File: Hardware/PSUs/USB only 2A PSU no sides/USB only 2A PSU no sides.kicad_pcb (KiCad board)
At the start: 4 copper layers, 45 x 20 mm, 46 parts, among them J10 G-Switch-GT-USB-7025, J11 1.27mm 4 pin socket, J12 USB, J3 Keystone 3579, J5 Keystone 3569, J7 Keystone 3579, J9 Keystone 3569, U1 AP63205WU, U2 AP63203WU, U5 THVD1420DRLR, U6 CH32X035G8U6, U7 TPS7A2633DRV

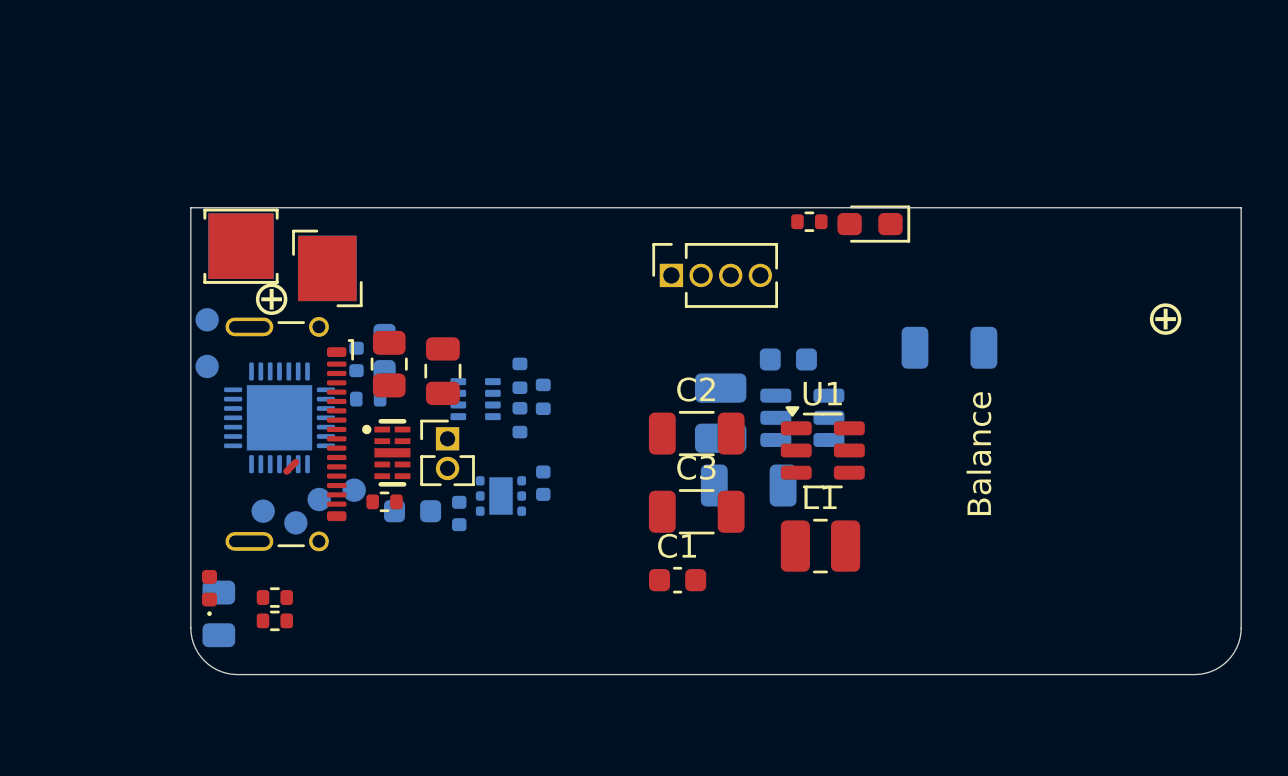
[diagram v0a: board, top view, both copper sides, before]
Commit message: Finished schematic, started arrangement
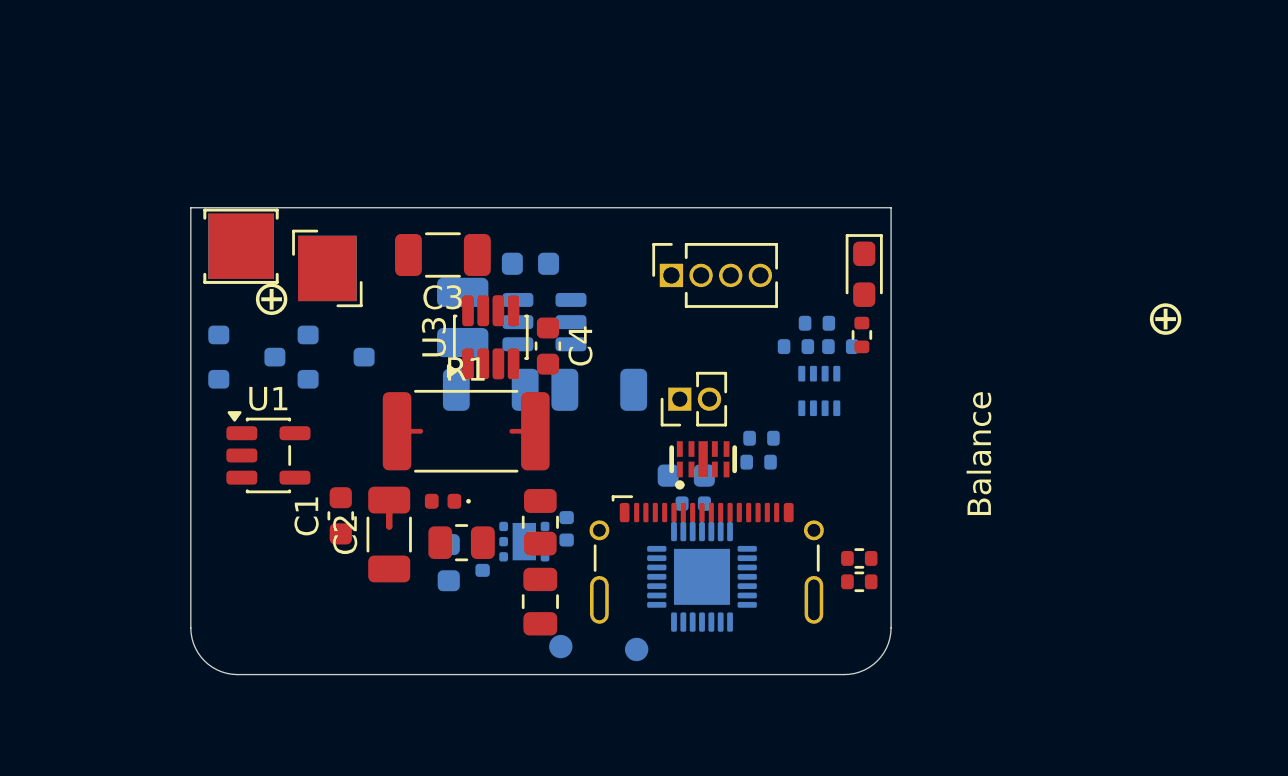
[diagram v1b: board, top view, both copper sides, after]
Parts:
- removed L1: 2.2uH, WIP322512A-2R2MLDG, Inductor_SMD:L_1008_2520Metric
- removed the TP2 at (115.1, 124.1)
- removed TP3: SCK, TestPoint:TestPoint_Pad_D1.0mm
- removed TP5: SDI, TestPoint:TestPoint_Pad_D1.0mm
- removed TP6: SDO, TestPoint:TestPoint_Pad_D1.0mm
- added C4: 100nF, 16v, Capacitor_SMD:C_0603_1608Metric, F.Cu at (123.4, 117.9)
- added NT1: NetTie_2, custom_Connector:NetTie-2_SMD_Pad0.2mm, F.Cu at (117.8, 121.6)
- added NT2: NetTie_2, custom_Connector:NetTie-2_SMD_Pad0.2mm, F.Cu at (122.0, 121.6)
- added Q1: PJA3430, or HL 2320A, Package_TO_SOT_SMD:SC-59, B.Cu at (114.3, 118.4)
- added Q2: PJA3430, or HL 2320A, Package_TO_SOT_SMD:SC-59, B.Cu at (110.5, 118.4)
- added R1: 50mOhm, Resistor_SMD:R_2512_6332Metric, F.Cu at (119.9, 121.6)
- added U3: INA219AxDCN, Package_TO_SOT_SMD:SOT-23-8, F.Cu at (121.0, 117.5)
- C1: value 100nF, 16v -> 10uF, 16v
- R19: moved to B.Cu
- R9: moved to F.Cu
- U1: value AP63205WU -> FAN3111E; footprint Package_TO_SOT_SMD:TSOT-23-6 -> Package_TO_SOT_SMD:SOT-23-5
- U4: renamed from U6; footprint Package_DFN_QFN:QFN-28-1EP_4x4mm_P0.4mm_EP2.8x2.8mm -> Package_DFN_QFN:QFN-28-1EP_4x4mm_P0.4mm_EP2.4x2.4mm
- moved R3 25.2 mm to (136.7, 127.0), turned to 0 degrees
- moved R4 25.0 mm to (136.7, 128.0), turned to 0 degrees
- moved U1 23.8 mm to (111.4, 122.6)
- moved TP2 22.0 mm to (127.2, 130.9), turned to -90 degrees
- moved TP1 20.6 mm to (124.0, 130.8), turned to -90 degrees
- moved J10 20.5 mm to (130.2, 128.5), turned to 0 degrees
- moved U4 19.3 mm to (130.0, 127.8), turned to -90 degrees
- moved R33 16.9 mm to (132.4, 122.9), turned to 180 degrees
- moved R19 16.4 mm to (132.6, 121.9)
- moved C5 15.7 mm to (129.6, 124.7), turned to 0 degrees
- moved C3 15.5 mm to (118.9, 114.0), turned to 180 degrees
- moved C28 15.1 mm to (125.6, 119.8)
- moved U5 14.7 mm to (135.0, 119.8), turned to 90 degrees
- moved C1 14.7 mm to (114.5, 125.2), turned to 90 degrees
- moved R28 14.1 mm to (135.9, 118.0), turned to 180 degrees
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- renumbered C25 to C5, C26 to C6, R11 to R3, R29 to R4, TP4 to TP1, TP1 to TP2
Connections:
- C1 pad 1: Net-(U1-BST) -> GND
- C1 pad 2: Net-(U1-SW) -> /Connectors/MOTORPWR
- C2 pad 1: /Connectors/USBPWR -> GND
- C2 pad 2: GND -> /Connectors/MOTORPWR
- C28 pad 1: /Connectors/USBPWR -> /Connectors/MOTORPWR
- C3 pad 1: /Connectors/MOTORPWR -> GNDPWR
- C3 pad 2: GND -> /Connectors/MOTORPWR
- J10 pad GND: GND -> (no net)
- NT12 pad 2: /Connectors/USBPWR -> /Connectors/MOTORPWR
- TP1 pad 1: /SDA -> Net-(U4-SWDIO/PC18)
- TP2 pad 1: /SCL -> Net-(U4-SWCLK/PC19)
- U1 pad 2: /MCU/5v PWRON -> GND
- U1 pad 3: /Connectors/USBPWR -> /MCU/5v EN
- U1 pad 4: GND -> /MCU/3.3v
- U1 pad 5: Net-(U1-SW) -> Net-(Q1-G)
- U2 pad 2: /MCU/3v3 PWRON -> /MCU/3v3 EN
- U2 pad 3: /Connectors/USBPWR -> /Connectors/MOTORPWR
- U4 pad 10: /MCU/SCLK -> /SCL
- U4 pad 11: /MCU/MISO -> /SDA
- U4 pad 12: /MCU/MOSI -> unconnected-(U4-ADC7/PA7-Pad12)
- U4 pad 14: unconnected-(U6-PB3-Pad14) -> /MCU/3v3 EN
- U4 pad 15: unconnected-(U6-PB4-Pad15) -> /MCU/5v EN
- U4 pad 17: /MCU/3v3 PWRON -> unconnected-(U4-PB6-Pad17)
- U4 pad 18: /MCU/5v PWRON -> unconnected-(U4-PB7-Pad18)
- U4 pad 24: /SCL -> Net-(U4-SWCLK/PC19)
- U4 pad 25: /SDA -> Net-(U4-SWDIO/PC18)
- U4 pad 9: /MCU/CS -> unconnected-(U4-ADC4/PA4-Pad9)
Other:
- board size 45 x 20 mm -> 30 x 20 mm
- copper layers 4 -> 2

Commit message: Added USB bus and finished preliminary routing
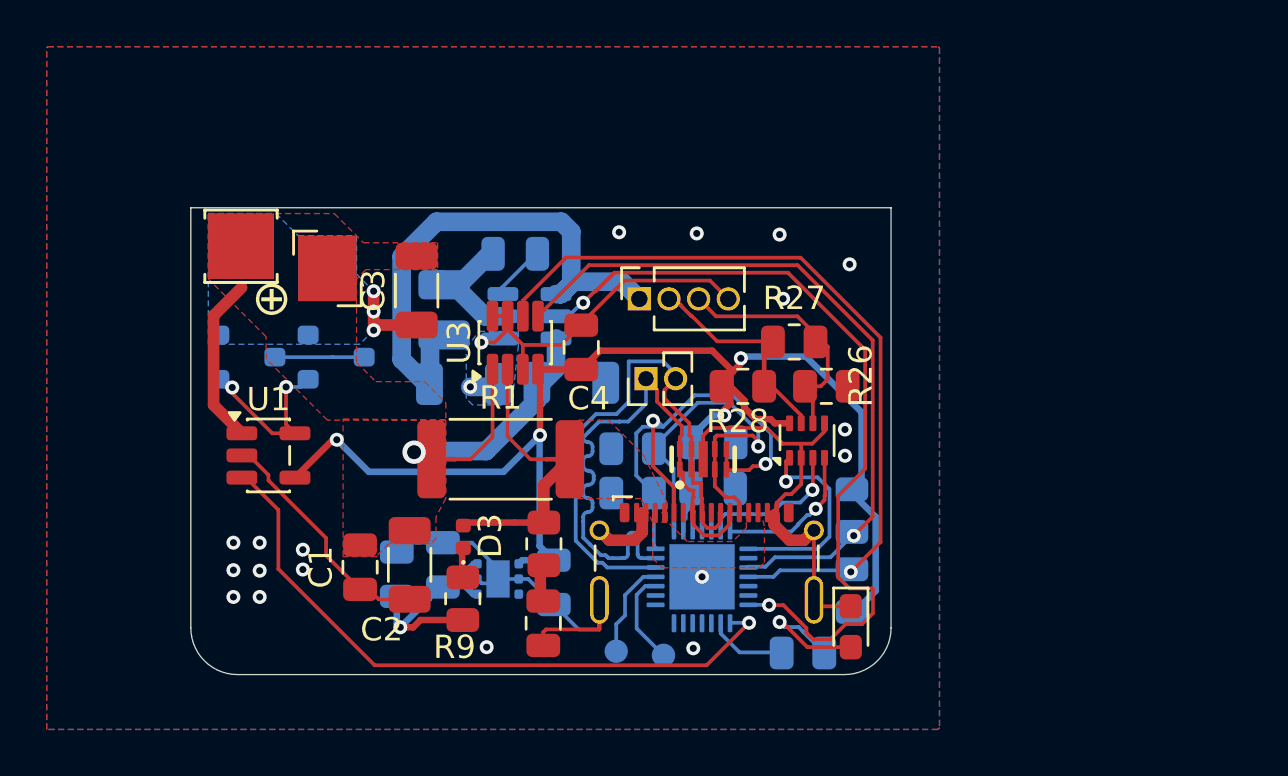
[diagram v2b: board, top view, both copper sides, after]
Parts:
- C1, C31, C4, C40, C6: footprint Capacitor_SMD:C_0603_1608Metric -> Capacitor_SMD:C_0805_2012Metric
- C32, C33, C5: footprint Capacitor_SMD:C_0402_1005Metric -> Capacitor_SMD:C_0805_2012Metric
- R19, R33: footprint Resistor_SMD:R_0402_1005Metric -> Resistor_SMD:R_0805_2012Metric
- R25, R3, R4: footprint Resistor_SMD:R_0402_1005Metric -> Resistor_SMD:R_0805_2012Metric; moved to B.Cu
- R26, R27, R28: footprint Resistor_SMD:R_0402_1005Metric -> Resistor_SMD:R_0805_2012Metric; moved to F.Cu
- U4: footprint Package_DFN_QFN:QFN-28-1EP_4x4mm_P0.4mm_EP2.4x2.4mm -> qfn_custom:QFN-28-1EP_4x4mm_P0.4mm_EP2.8x2.8mm
- U5: moved to F.Cu
- moved D4 15.1 mm to (136.4, 129.9)
- moved R25 13.9 mm to (134.3, 131.1), turned to 0 degrees
- moved NT12 5.65 mm to (122.2, 125.5), turned to 0 degrees
- moved R33 5.56 mm to (127.0, 124.2), turned to 0 degrees
- moved R19 5.54 mm to (127.0, 122.3), turned to 0 degrees
- moved R28 4.51 mm to (131.8, 119.7), turned to 0 degrees
- moved R9 2.40 mm to (119.8, 128.8), turned to 90 degrees
- moved TP1 2.38 mm to (126.3, 131.0)
- moved C33 2.36 mm to (123.7, 128.1)
- moved C1 2.35 mm to (115.3, 127.4)
- moved C31 2.28 mm to (116.9, 127.7), turned to 90 degrees
- moved U5 2.19 mm to (134.5, 122.0)
- moved R26 2.14 mm to (135.3, 119.7), turned to 0 degrees
- moved R3 2.07 mm to (136.4, 125.0), turned to 90 degrees
- moved U7 1.96 mm to (121.3, 127.9)
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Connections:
- C1 pad 2: /Connectors/MOTORPWR -> /PSU/5V Out
- C2 pad 2: /Connectors/MOTORPWR -> /PSU/5V Out
- C28 pad 1: /Connectors/MOTORPWR -> /PSU/5V Out
- C3 pad 2: /Connectors/MOTORPWR -> /PSU/5V Out
- C31 pad 1: /PSU/Always On PWR -> Net-(U7-EN)
- C32 pad 1: /PSU/Always On PWR -> Net-(U7-EN)
- C4 pad 2: /PSU/Always On PWR -> /MCU/3.3v
- J3 pad 1: /Connectors/MOTORPWR -> /PSU/5V Out
- J5 pad 1: /Connectors/MOTORPWR -> /PSU/5V Out
- J7 pad 1: GND -> GNDPWR
- J9 pad 1: GND -> GNDPWR
- NT1 pad 2: /Connectors/MOTORPWR -> /PSU/5V Out
- NT12 pad 2: /Connectors/MOTORPWR -> /Connectors/USBPWR
- R1 pad 1: /Connectors/MOTORPWR -> /PSU/5V Out
- R9 pad 1: /PSU/Always On PWR -> Net-(U7-EN)
- U1 pad 1: /Connectors/MOTORPWR -> /PSU/5V Out
- U2 pad 3: /Connectors/MOTORPWR -> /PSU/5V Out
- U3 pad 4: /PSU/Always On PWR -> /MCU/3.3v
- U7 pad 4: /PSU/Always On PWR -> Net-(U7-EN)
- U7 pad 6: /PSU/Always On PWR -> Net-(U7-EN)
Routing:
- net GND: track 0.00 -> 74.9 mm, vias 0 -> 20
- net /MCU/3.3v: track 0.00 -> 60.2 mm, vias 0 -> 4
- net /MCU/3v3 EN: track 0.00 -> 35.1 mm, vias 0 -> 2
- net /SDA: track 0.00 -> 33.3 mm, vias 0 -> 1
- net /SCL: track 0.00 -> 30.5 mm, vias 0 -> 1
- net /MCU/5v EN: track 0.00 -> 28.1 mm, vias 0 -> 1
- net /Connectors/D+: track 0.00 -> 26.0 mm
- net /Connectors/D-: track 0.00 -> 24.7 mm
- net /Connectors/3.3v: track 0.00 -> 23.5 mm
- net /Connectors/CC1: track 0.00 -> 21.8 mm, vias 0 -> 2
- net /Connectors/CC2: track 0.00 -> 16.8 mm, vias 0 -> 1
- net /PSU/5V Out: track 0.00 -> 16.5 mm, vias 0 -> 1
- net /Connectors/RS485-: track 0.00 -> 10.9 mm
- net /Connectors/RS485+: track 0.00 -> 10.2 mm
- net Net-(U7-EN): track 0.00 -> 9.75 mm, vias 0 -> 1
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- added copper zone on F.Cu, net /Connectors/USBPWR
- added copper zone on F.Cu, net /PSU/5V Out
- added copper zone on B.Cu, net GND
- added copper zone on F.Cu, net GND
- added copper zone on B.Cu, net GNDPWR
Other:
- board text added: "©2025 Asher Edwards"
- board text removed: "2s 40A PSU"
- board text removed: "BAT+"
- board text removed: "BAT-"
- board text removed: "Balance"
- board text removed: "©2024 Asher Edwards"

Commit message: revised ground circuit
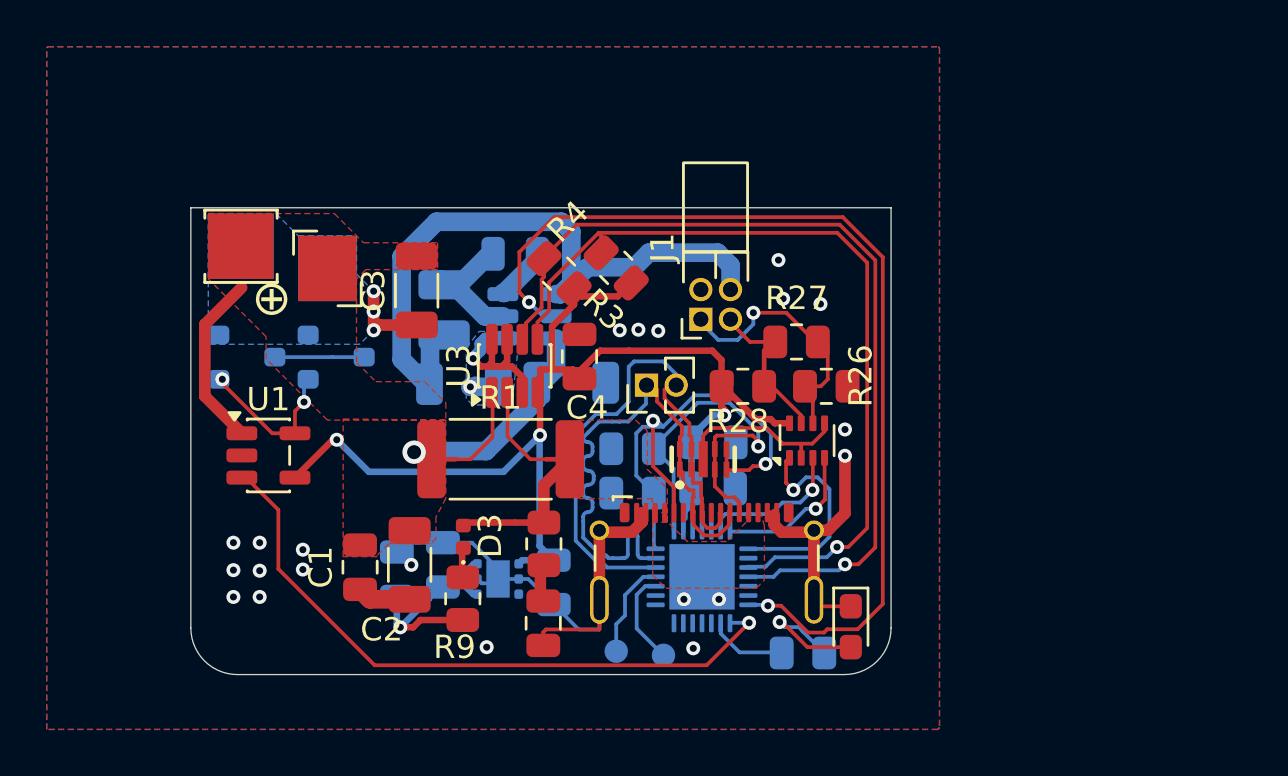
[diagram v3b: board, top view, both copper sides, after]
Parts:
- removed J11: 1.27mm 4 pin socket, Connector_PinSocket_1.27mm:PinSocket_1x04_P1.27mm_Vertical
- added J1: Precidip 853-83-004-20-001101, custom_Connector:PinSocket_2x02_P1.27mm_Horizontal, F.Cu at (129.9, 116.8)
- R3, R4: moved to F.Cu
- moved R4 18.5 mm to (123.9, 114.8), turned to -45 degrees
- moved R3 14.5 mm to (126.3, 114.6), turned to -45 degrees
- moved U3 0.99 mm to (122.0, 118.8)
- moved C4 0.40 mm to (124.8, 118.4)
- moved J12 0.28 mm to (127.6, 119.6)
- moved R27 0.10 mm to (134.1, 117.8)
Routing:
- net GND: track 74.9 -> 63.0 mm, vias 20 -> 23
- net /MCU/3.3v: track 60.2 -> 51.5 mm, vias 4 -> 3
- net /MCU/3v3 EN: track 35.1 -> 42.2 mm
- net /Connectors/3.3v: track 23.5 -> 28.9 mm
- net /SCL: track 30.5 -> 35.8 mm
- net /SDA: track 33.3 -> 37.6 mm
- net /Connectors/RS485+: track 10.2 -> 7.72 mm
- net /Connectors/RS485-: track 10.9 -> 11.9 mm, vias 0 -> 1
- net Net-(U3-IN-): track 4.94 -> 3.95 mm
- net Net-(U3-IN+): track 4.90 -> 3.92 mm
- net Net-(Q1-G): track 7.59 -> 6.87 mm
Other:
- board text added: "D- D+"

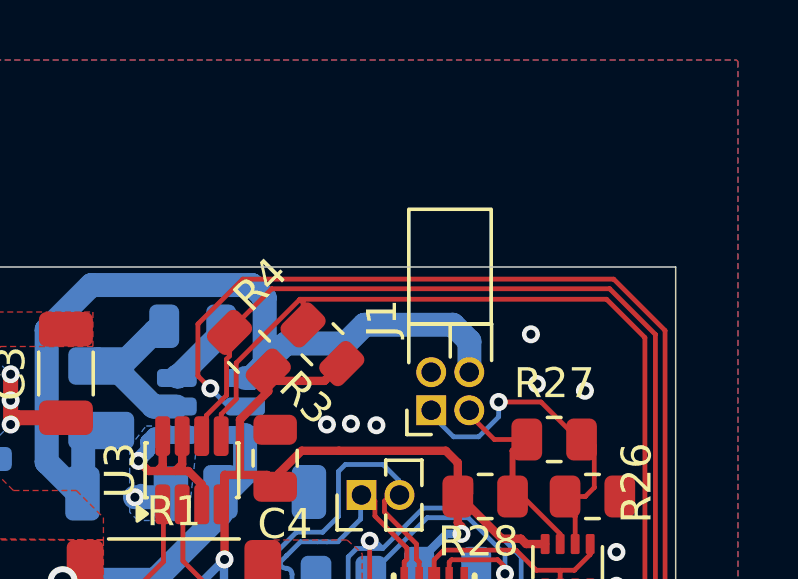
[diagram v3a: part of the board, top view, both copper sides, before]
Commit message: Updated connector part ID, added production files
I messed on on a single number 83 vs 87. The difference is in the plating, and 83 is not available anywhere
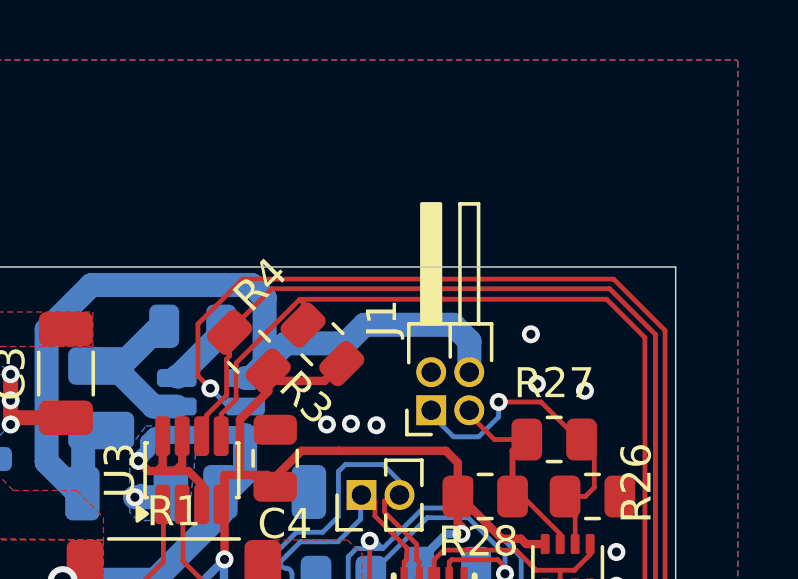
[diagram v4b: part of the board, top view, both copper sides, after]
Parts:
- J1: value Precidip 853-83-004-20-001101 -> Precidip 853-87-004-20-001101; footprint custom_Connector:PinSocket_2x02_P1.27mm_Horizontal -> Connector_PinHeader_1.27mm:PinHeader_2x02_P1.27mm_Horizontal
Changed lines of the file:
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@@
 	(paper "A4")
 	(title_block
-		(title "CACKLE 2s 40A PSU & Charger")
+		(title "USB only 2A PSU")
 		(date "2024-12-23")
 		(rev "V1")
@@
 		)
 	)
-	(footprint "custom_Connector:PinSocket_2x02_P1.27mm_Horizontal"
+	(footprint "Connector_PinHeader_1.27mm:PinHeader_2x02_P1.27mm_Horizontal"
 		(layer "F.Cu")
 		(at 129.95 116.775 90)
@@
 			)
 		)
-		(property "Value" "Precidip 853-83-004-20-001101"
+		(property "Value" "Precidip 853-87-004-20-001101"
 			(at 3.0675 2.905 90)
 			(layer "F.Fab")
@@
 			)
 		)
-		(property "Datasheet" ""
+		(property "Datasheet" "~"
 			(at 0 0 90)
 			(layer "F.Fab")
@@
 			)
 		)
-		(property "Description" ""
+		(property "Description" "Generic connector, double row, 02x02, odd/even pin numbering scheme (row 1 odd numbers, row 2 even numbers), script generated (kicad-library-utils/schlib/autogen/connector/)"
 			(at 0 0 90)
 			(layer "F.Fab")
@@
 		)
 		(fp_line
+			(start 6.88 0.96)
+			(end 6.88 1.58)
+			(stroke
+				(width 0.12)
+				(type solid)
+			)
+			(layer "F.SilkS")
+		)
+		(fp_line
+			(start 2.88 0.96)
+			(end 6.88 0.96)
+			(stroke
+				(width 0.12)
+				(type solid)
+			)
+			(layer "F.SilkS")
+		)
+		(fp_line
+			(start 6.88 1.58)
+			(end 2.88 1.58)
+			(stroke
+				(width 0.12)
+				(type solid)
+			)
+			(layer "F.SilkS")
+		)
+		(fp_line
 			(start 2.88 2.015)
 			(end 1.66 2.015)
@@
 		)
 		(fp_rect
-			(start 2.88 -0.745)
-			(end 6.7 2)
+			(start 2.88 -0.31)
+			(end 6.88 0.31)
 			(stroke
 				(width 0.12)
-				(type default)
+				(type solid)
 			)
-			(fill no)
+			(fill yes)
 			(layer "F.SilkS")
 		)
@@
 		)
 		(fp_line
+			(start 6.77 -0.2)
+			(end 6.77 0.2)
+			(stroke
+				(width 0.1)
+				(type solid)
+			)
+			(layer "F.Fab")
+		)
+		(fp_line
+			(start 2.77 -0.2)
+			(end 6.77 -0.2)
+			(stroke
+				(width 0.1)
+				(type solid)
+			)
+			(layer "F.Fab")
+		)
+		(fp_line
 			(start -0.2 -0.2)
 			(end 1.77 -0.2)
@@
 		)
 		(fp_line
+			(start 2.77 0.2)
+			(end 6.77 0.2)
+			(stroke
+				(width 0.1)
+				(type solid)
+			)
+			(layer "F.Fab")
+		)
+		(fp_line
 			(start -0.2 0.2)
 			(end 1.77 0.2)
@@
 		)
 		(fp_line
+			(start 6.77 1.07)
+			(end 6.77 1.47)
+			(stroke
+				(width 0.1)
+				(type solid)
+			)
+			(layer "F.Fab")
+		)
+		(fp_line
+			(start 2.77 1.07)
+			(end 6.77 1.07)
+			(stroke
+				(width 0.1)
+				(type solid)
+			)
+			(layer "F.Fab")
+		)
+		(fp_line
 			(start -0.2 1.07)
 			(end 1.77 1.07)
@@
 		)
 		(fp_line
+			(start 2.77 1.47)
+			(end 6.77 1.47)
+			(stroke
+				(width 0.1)
+				(type solid)
+			)
+			(layer "F.Fab")
+		)
+		(fp_line
 			(start -0.2 1.47)
 			(end 1.77 1.47)
@@
 			(layer "F.Fab")
 		)
-		(fp_rect
-			(start 2.88 -0.745)
-			(end 6.7 2)
-			(stroke
-				(width 0.12)
-				(type solid)
-			)
-			(fill no)
-			(layer "F.Fab")
-		)
 		(fp_text user "${REFERENCE}"
 			(at 2.27 0.635 180)
@@
 			(thermal_gap 0.5)
 			(thermal_bridge_width 0.5)
-			(smoothing fillet)
-			(radius 0.2)
 		)
 		(polygon
